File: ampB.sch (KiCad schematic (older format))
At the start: 9 parts, among them U2 Mux, U3 MCP6004

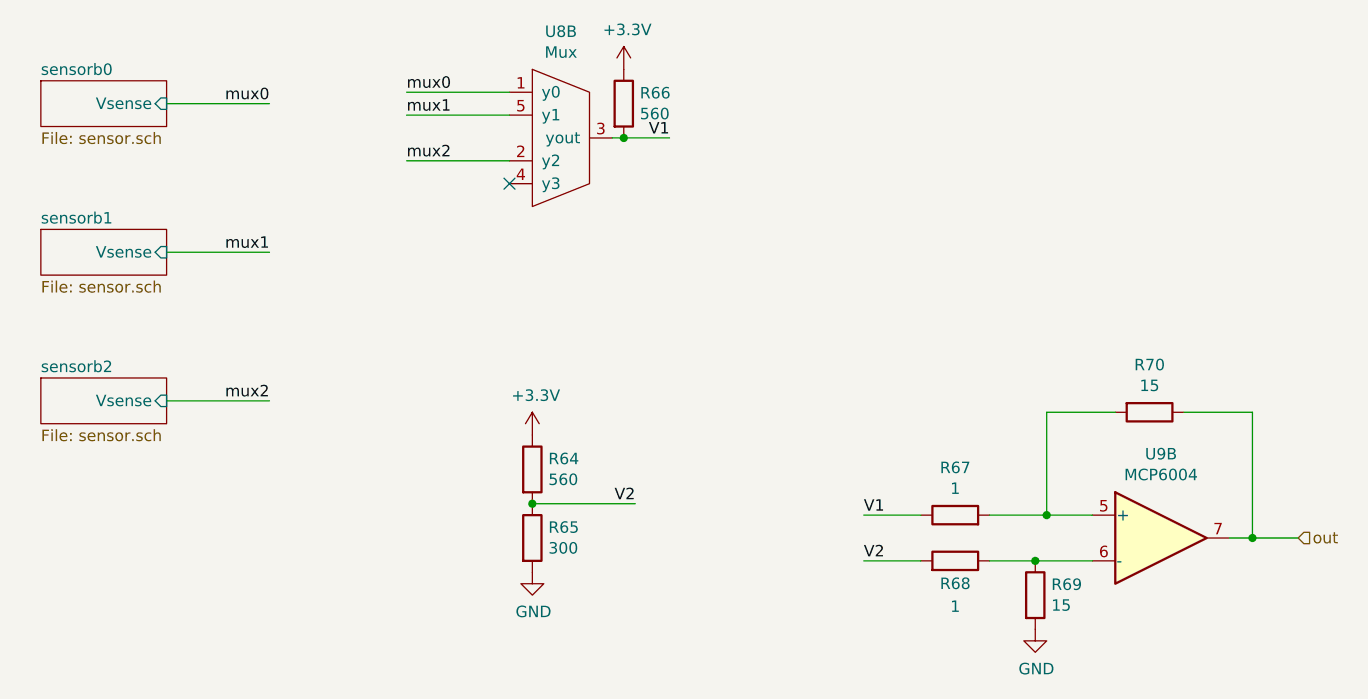
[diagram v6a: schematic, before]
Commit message: switched over remaining rs to 0805
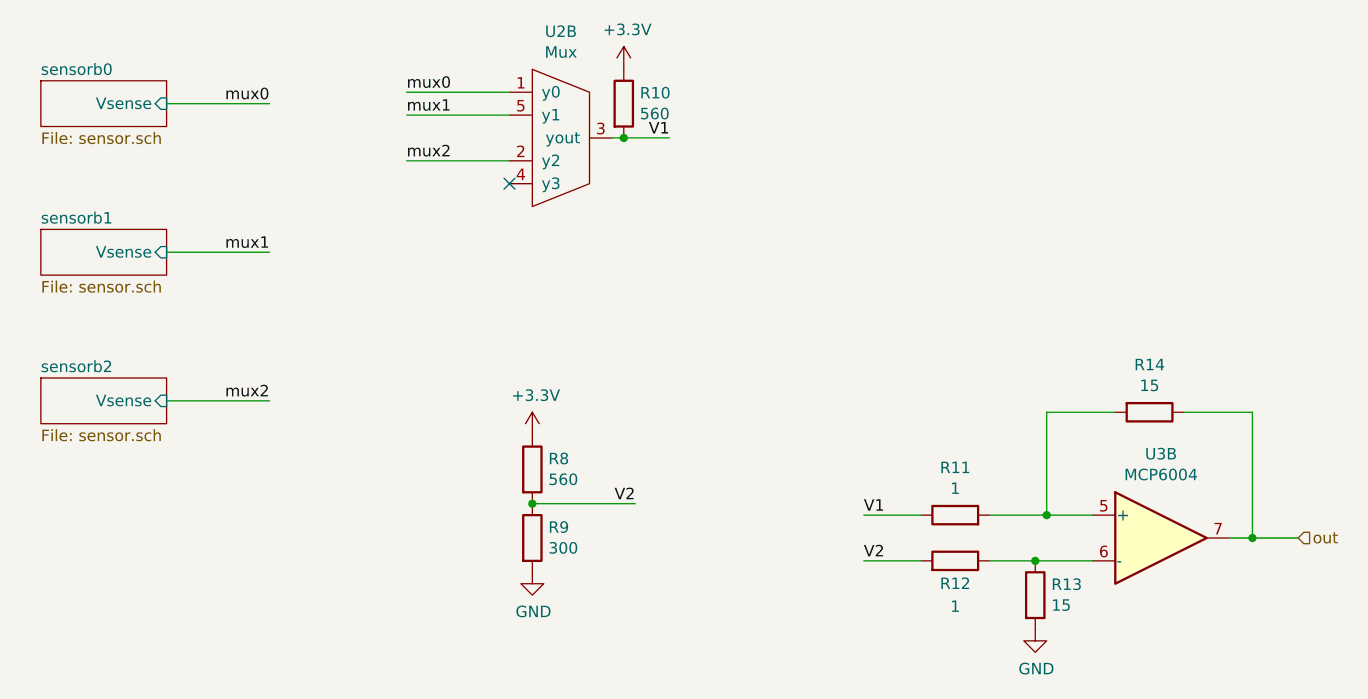
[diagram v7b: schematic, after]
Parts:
- R10, R11, R12, R13, R14, R8, R9: footprint Resistor_THT:R_Axial_DIN0204_L3.6mm_D1.6mm_P5.08mm_Horizontal -> Resistor_SMD:R_0805_2012Metric_Pad1.20x1.40mm_HandSolder
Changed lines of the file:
@@
 AR Path="/601B4C11/6019E3A5" Ref="R41"  Part="1"
 AR Path="/601B73BA/6019E3A5" Ref="R69"  Part="1"
-F 0 "R69" H 5520 4096 50  0000 L CNN
+F 0 "R13" H 5520 4096 50  0000 L CNN
 F 1 "15" H 5520 4005 50  0000 L CNN
-F 2 "Resistor_THT:R_Axial_DIN0204_L3.6mm_D1.6mm_P5.08mm_Horizontal" V 5380 4050 50  0001 C CNN
+F 2 "Resistor_SMD:R_0805_2012Metric_Pad1.20x1.40mm_HandSolder" V 5380 4050 50  0001 C CNN
 F 3 "~" H 5450 4050 50  0001 C CNN
 	1    5450 4050
@@
 AR Path="/601B4C11/6017E430" Ref="R42"  Part="1"
 AR Path="/601B73BA/6017E430" Ref="R70"  Part="1"
-F 0 "R70" V 5743 3250 50  0000 C CNN
+F 0 "R14" V 5743 3250 50  0000 C CNN
 F 1 "15" V 5834 3250 50  0000 C CNN
-F 2 "Resistor_THT:R_Axial_DIN0204_L3.6mm_D1.6mm_P5.08mm_Horizontal" V 5880 3250 50  0001 C CNN
+F 2 "Resistor_SMD:R_0805_2012Metric_Pad1.20x1.40mm_HandSolder" V 5880 3250 50  0001 C CNN
 F 3 "~" H 5950 3250 50  0001 C CNN
 	1    5950 3250
@@
 AR Path="/601B4C11/60198F33" Ref="R39"  Part="1"
 AR Path="/601B73BA/60198F33" Ref="R67"  Part="1"
-F 0 "R67" V 5307 3700 50  0000 C CNN
+F 0 "R11" V 5307 3700 50  0000 C CNN
 F 1 "1" V 5216 3700 50  0000 C CNN
-F 2 "Resistor_THT:R_Axial_DIN0204_L3.6mm_D1.6mm_P5.08mm_Horizontal" V 5030 3700 50  0001 C CNN
+F 2 "Resistor_SMD:R_0805_2012Metric_Pad1.20x1.40mm_HandSolder" V 5030 3700 50  0001 C CNN
 F 3 "~" H 5100 3700 50  0001 C CNN
 	1    5100 3700
@@
 AR Path="/601B4C11/6017E432" Ref="R40"  Part="1"
 AR Path="/601B73BA/6017E432" Ref="R68"  Part="1"
-F 0 "R68" V 5000 3900 50  0000 C CNN
+F 0 "R12" V 5000 3900 50  0000 C CNN
 F 1 "1" V 4900 3900 50  0000 C CNN
-F 2 "Resistor_THT:R_Axial_DIN0204_L3.6mm_D1.6mm_P5.08mm_Horizontal" V 5030 3900 50  0001 C CNN
+F 2 "Resistor_SMD:R_0805_2012Metric_Pad1.20x1.40mm_HandSolder" V 5030 3900 50  0001 C CNN
 F 3 "~" H 5100 3900 50  0001 C CNN
 	1    5100 3900
@@
 AR Path="/601B4C11/60198F35" Ref="R36"  Part="1"
 AR Path="/601B73BA/60198F35" Ref="R64"  Part="1"
-F 0 "R64" H 3320 3546 50  0000 L CNN
+F 0 "R8" H 3320 3546 50  0000 L CNN
 F 1 "560" H 3320 3455 50  0000 L CNN
-F 2 "Resistor_THT:R_Axial_DIN0204_L3.6mm_D1.6mm_P5.08mm_Horizontal" V 3180 3500 50  0001 C CNN
+F 2 "Resistor_SMD:R_0805_2012Metric_Pad1.20x1.40mm_HandSolder" V 3180 3500 50  0001 C CNN
 F 3 "~" H 3250 3500 50  0001 C CNN
 	1    3250 3500
@@
 AR Path="/601B4C11/6019E3B4" Ref="R37"  Part="1"
 AR Path="/601B73BA/6019E3B4" Ref="R65"  Part="1"
-F 0 "R65" H 3320 3846 50  0000 L CNN
+F 0 "R9" H 3320 3846 50  0000 L CNN
 F 1 "300" H 3320 3755 50  0000 L CNN
-F 2 "Resistor_THT:R_Axial_DIN0204_L3.6mm_D1.6mm_P5.08mm_Horizontal" V 3180 3800 50  0001 C CNN
+F 2 "Resistor_SMD:R_0805_2012Metric_Pad1.20x1.40mm_HandSolder" V 3180 3800 50  0001 C CNN
 F 3 "~" H 3250 3800 50  0001 C CNN
 	1    3250 3800
@@
 AR Path="/601B4C11/6019E3B5" Ref="#PWR053"  Part="1"
 AR Path="/601B73BA/6019E3B5" Ref="#PWR087"  Part="1"
-F 0 "#PWR087" H 3250 3200 50  0001 C CNN
+F 0 "#PWR019" H 3250 3200 50  0001 C CNN
 F 1 "+3.3V" H 3265 3523 50  0000 C CNN
 F 2 "" H 3250 3350 50  0001 C CNN
@@
 AR Path="/601B4C11/6017E436" Ref="#PWR054"  Part="1"
 AR Path="/601B73BA/6017E436" Ref="#PWR088"  Part="1"
-F 0 "#PWR088" H 3250 3700 50  0001 C CNN
+F 0 "#PWR020" H 3250 3700 50  0001 C CNN
 F 1 "GND" H 3255 3777 50  0000 C CNN
 F 2 "" H 3250 3950 50  0001 C CNN
@@
 AR Path="/601B4C11/6019E3AC" Ref="#PWR056"  Part="1"
 AR Path="/601B73BA/6019E3AC" Ref="#PWR090"  Part="1"
-F 0 "#PWR090" H 5450 3950 50  0001 C CNN
+F 0 "#PWR022" H 5450 3950 50  0001 C CNN
 F 1 "GND" H 5455 4027 50  0000 C CNN
 F 2 "" H 5450 4200 50  0001 C CNN
@@
 AR Path="/601B4C11/6017859B" Ref="U5"  Part="2"
 AR Path="/601B73BA/6017859B" Ref="U8"  Part="2"
-F 0 "U8" H 3375 2515 50  0000 C CNN
+F 0 "U2" H 3375 2515 50  0000 C CNN
 F 1 "Mux" H 3375 2424 50  0000 C CNN
 F 2 "Package_SO:SOIC-16_3.9x9.9mm_P1.27mm" H 3350 2050 50  0001 C CNN
@@
 AR Path="/601B4C11/6018C8DB" Ref="U6"  Part="2"
 AR Path="/601B73BA/6018C8DB" Ref="U9"  Part="2"
-F 0 "U9" H 6000 4167 50  0000 C CNN
+F 0 "U3" H 6000 4167 50  0000 C CNN
 F 1 "MCP6004" H 6000 4076 50  0000 C CNN
 F 2 "Package_SO:SOIC-16_3.9x9.9mm_P1.27mm" H 5950 3900 50  0001 C CNN
@@
 AR Path="/601B4C11/602069C8" Ref="R38"  Part="1"
 AR Path="/601B73BA/602069C8" Ref="R66"  Part="1"
-F 0 "R66" H 3720 1946 50  0000 L CNN
+F 0 "R10" H 3720 1946 50  0000 L CNN
 F 1 "560" H 3720 1855 50  0000 L CNN
-F 2 "Resistor_THT:R_Axial_DIN0204_L3.6mm_D1.6mm_P5.08mm_Horizontal" V 3580 1900 50  0001 C CNN
+F 2 "Resistor_SMD:R_0805_2012Metric_Pad1.20x1.40mm_HandSolder" V 3580 1900 50  0001 C CNN
 F 3 "~" H 3650 1900 50  0001 C CNN
 	1    3650 1900
@@
 AR Path="/601B4C11/60206B01" Ref="#PWR055"  Part="1"
 AR Path="/601B73BA/60206B01" Ref="#PWR089"  Part="1"
-F 0 "#PWR089" H 3650 1600 50  0001 C CNN
+F 0 "#PWR021" H 3650 1600 50  0001 C CNN
 F 1 "+3.3V" H 3665 1923 50  0000 C CNN
 F 2 "" H 3650 1750 50  0001 C CNN

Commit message: fixed issue with wrong amp footprint
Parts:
- U3: footprint Package_SO:SOIC-16_3.9x9.9mm_P1.27mm -> Package_SO:SOIC-14_3.9x8.7mm_P1.27mm
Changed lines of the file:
@@
 F 0 "U3" H 6000 4167 50  0000 C CNN
 F 1 "MCP6004" H 6000 4076 50  0000 C CNN
-F 2 "Package_SO:SOIC-16_3.9x9.9mm_P1.27mm" H 5950 3900 50  0001 C CNN
+F 2 "Package_SO:SOIC-14_3.9x8.7mm_P1.27mm" H 5950 3900 50  0001 C CNN
 F 3 "http://ww1.microchip.com/downloads/en/DeviceDoc/21733j.pdf" H 6050 4000 50  0001 C CNN
 	2    6000 3800
